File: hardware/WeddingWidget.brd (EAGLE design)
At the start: 25.1 x 50.8 mm, 7 parts, among them J1 AVR_SPI_PRG_6NS, SW1 EVQQ2, SW2 EVQQ2

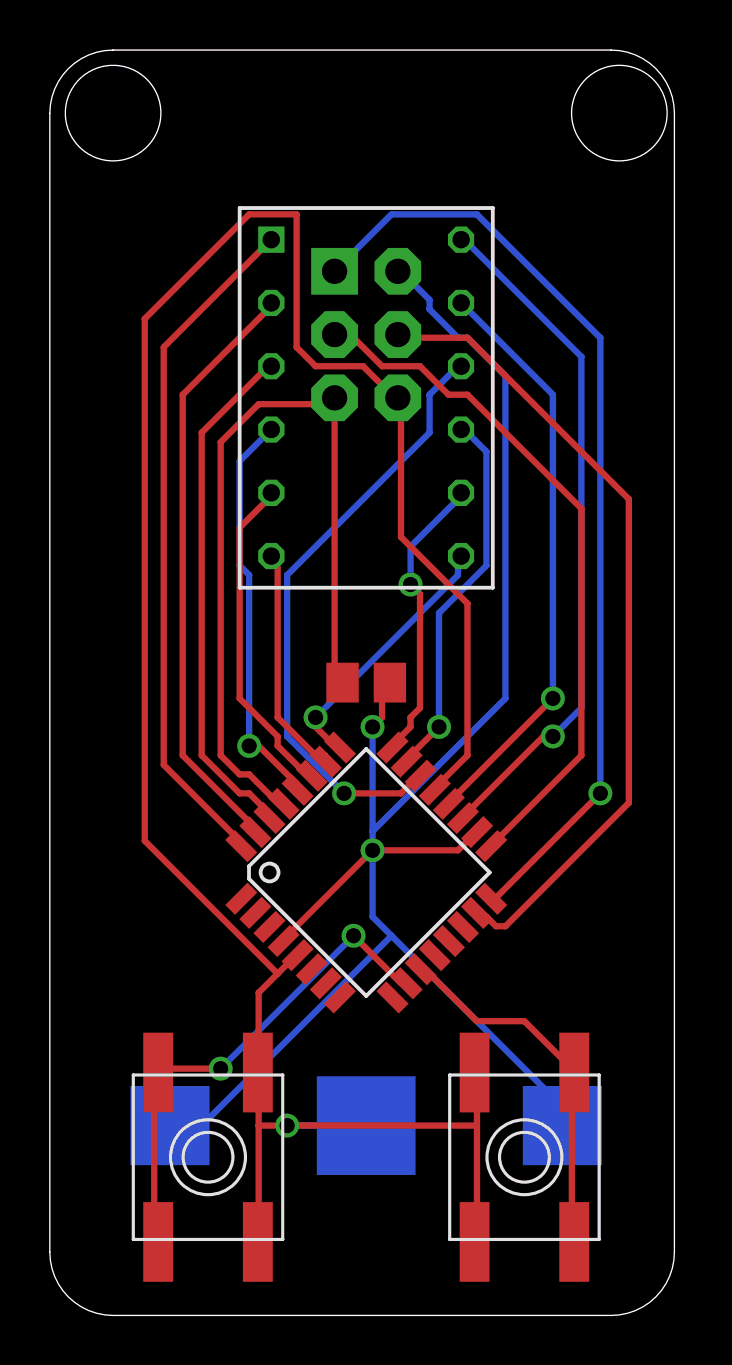
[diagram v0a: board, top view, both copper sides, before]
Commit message: added battery holder and bottom ground plane
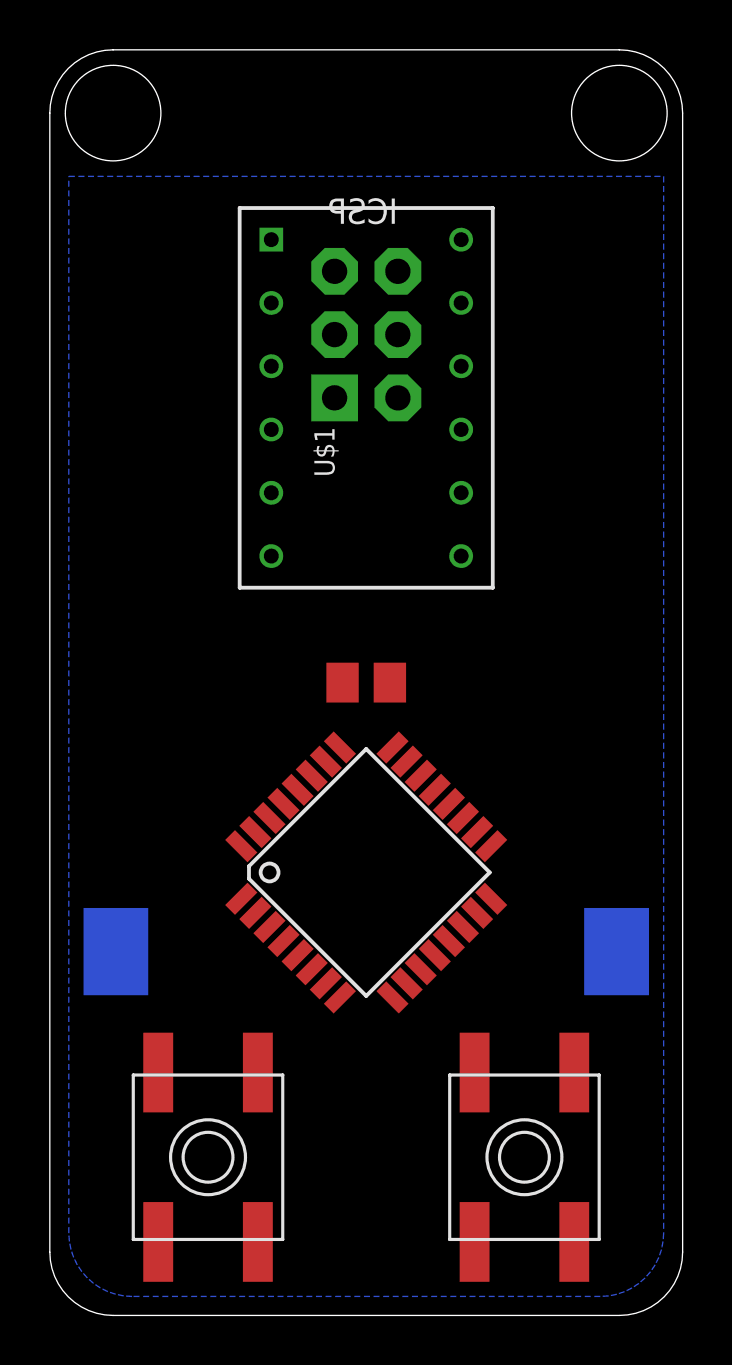
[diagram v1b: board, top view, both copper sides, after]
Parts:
- BAT1: device SparkFun:BATTCON_12MM -> rxtx-labs:BATTCON_12MM
- moved BAT1 6.99 mm to (12.7, 14.6), turned to 0 degrees
- flipped J1 to the bottom, turned to 90 degrees
- turned SW1 to 270 degrees
- turned SW2 to 90 degrees
- renumbered LED1 to U$1
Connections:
- net VCC: now also BAT1.V+; no longer BAT1.PWR@1, BAT1.PWR@2
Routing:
- net GND: track 95.0 -> 0.00 mm, vias 1 -> 0
- net VCC: track 69.7 -> 0.00 mm, vias 2 -> 0
- net MISO: track 38.1 -> 0.00 mm, vias 1 -> 0
- net RST: track 32.7 -> 0.00 mm
- net MOSI: track 32.5 -> 0.00 mm
- net SCK: track 27.9 -> 0.00 mm
- net ROW1: track 27.4 -> 0.00 mm, vias 1 -> 0
- net COL1: track 27.4 -> 0.00 mm
- net COL3: track 24.5 -> 0.00 mm, vias 1 -> 0
- net ROW3: track 24.0 -> 0.00 mm
- net ROW2: track 23.4 -> 0.00 mm, vias 1 -> 0
- net COL2: track 20.7 -> 0.00 mm
- net PCINT22: track 20.0 -> 0.00 mm, vias 2 -> 0
- net ROW5: track 16.2 -> 0.00 mm, vias 1 -> 0
- net ROW4: track 15.1 -> 0.00 mm, vias 1 -> 0
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- added copper zone on layer 16, net GND
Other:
- board size 25.1 x 50.8 mm -> 25.4 x 50.8 mm
- board text added: "ICSP"

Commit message: Hand routed all traces. Ready for prototype boards to be produced.
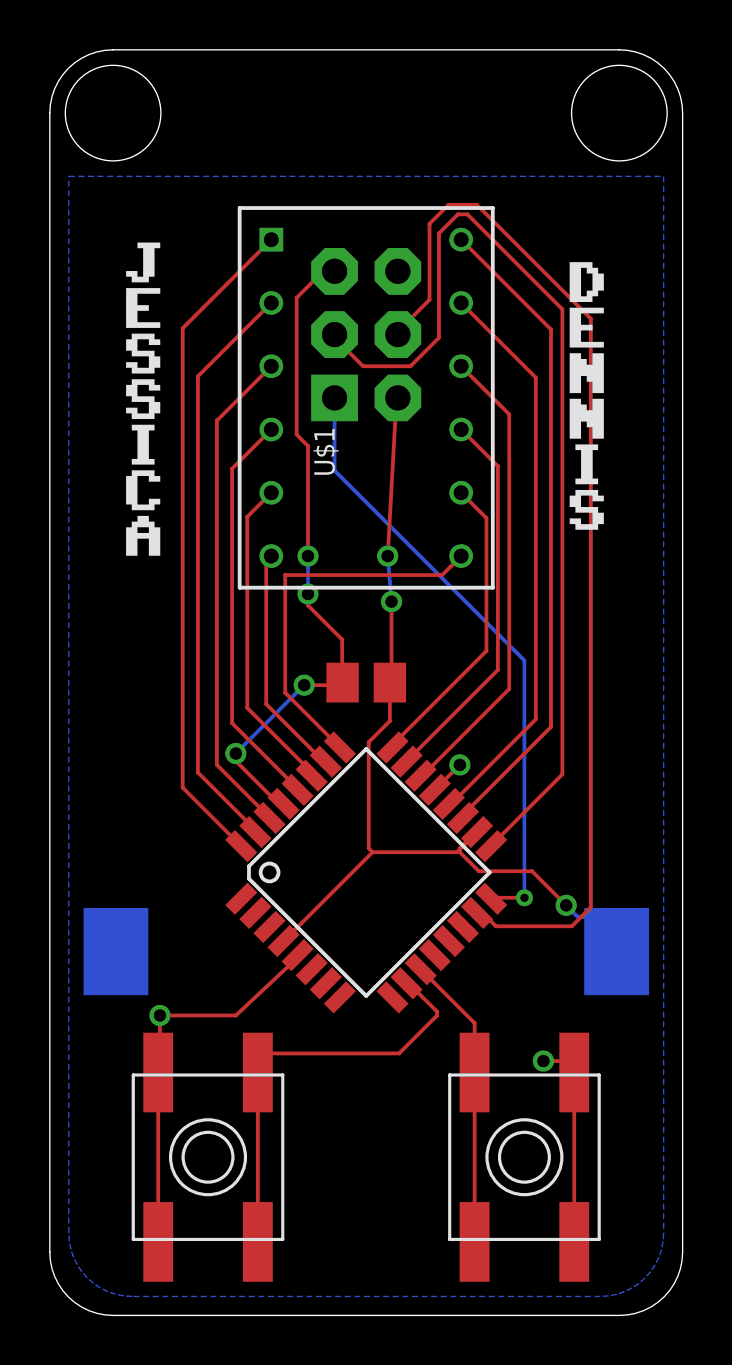
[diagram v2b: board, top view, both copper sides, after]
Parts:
- added U$2: DENNIS, rxtx-labs:DENNIS
- added U$3: JESSICA, rxtx-labs:JESSICA
- added U$4: 23FEB2013, rxtx-labs:23FEB2013
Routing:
- net MOSI: track 0.00 -> 42.3 mm
- net SCK: track 0.00 -> 39.0 mm
- net VCC: track 0.00 -> 38.1 mm, vias 0 -> 3
- net RST: track 0.00 -> 27.1 mm, vias 0 -> 4
- net COL1: track 0.00 -> 26.8 mm
- net ROW1: track 0.00 -> 26.2 mm
- net GND: track 0.00 -> 25.6 mm, vias 0 -> 3
- net MISO: track 0.00 -> 24.6 mm, vias 0 -> 1
- net ROW3: track 0.00 -> 23.4 mm
- net ROW2: track 0.00 -> 22.8 mm
- net COL2: track 0.00 -> 19.9 mm
- net COL3: track 0.00 -> 18.7 mm
- net PCINT22: track 0.00 -> 17.1 mm
- net ROW5: track 0.00 -> 16.2 mm
- net ROW4: track 0.00 -> 15.5 mm
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
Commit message: Dropped bitmapped text for prototype run.
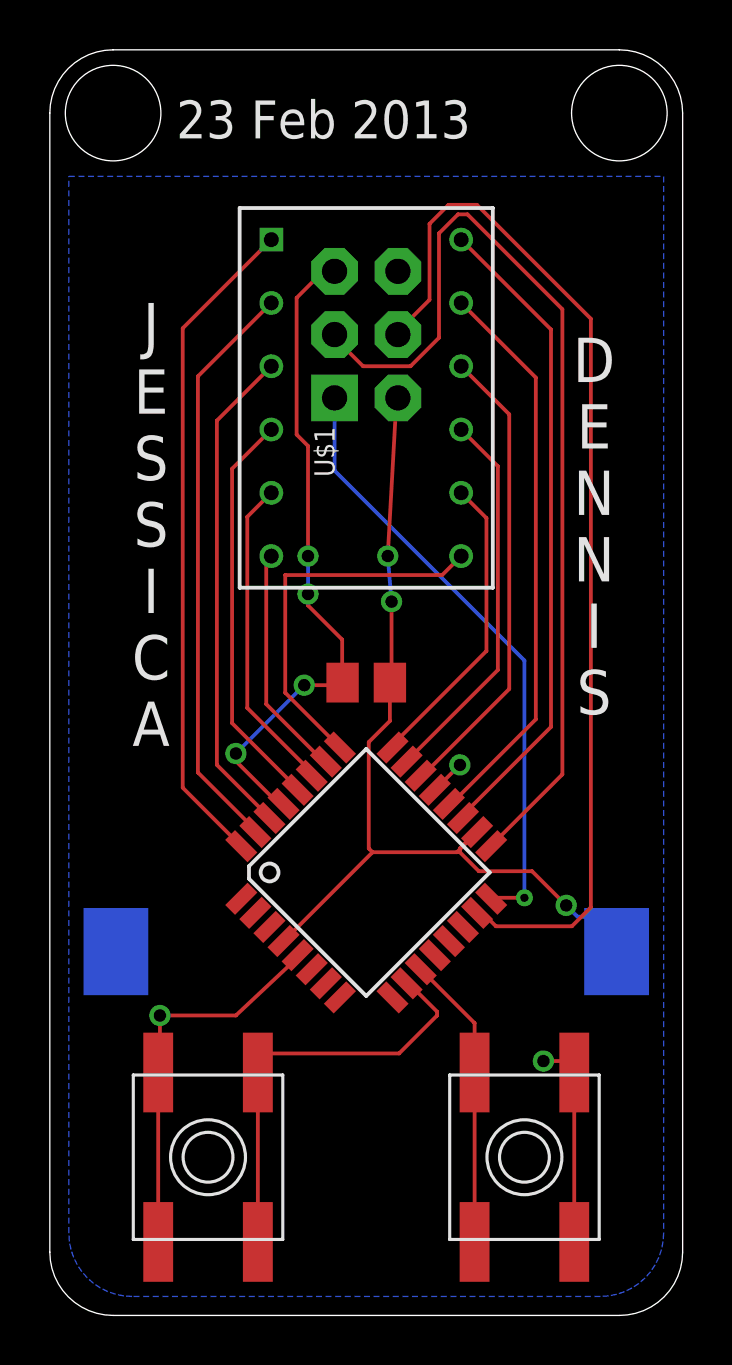
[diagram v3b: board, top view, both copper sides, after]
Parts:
- removed U$2: DENNIS, rxtx-labs:DENNIS
- removed U$3: JESSICA, rxtx-labs:JESSICA
- removed U$4: 23FEB2013, rxtx-labs:23FEB2013
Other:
- board text added: "23 Feb 2013"
- board text added: "D E N N I S"
- board text added: "J E S S I C A"
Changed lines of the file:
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@@
 <layer number="42" name="bRestrict" color="1" fill="10" visible="no" active="yes"/>
 <layer number="43" name="vRestrict" color="2" fill="10" visible="no" active="yes"/>
-<layer number="44" name="Drills" color="7" fill="1" visible="no" active="yes"/>
+<layer number="44" name="Drills" color="7" fill="1" visible="yes" active="yes"/>
 <layer number="45" name="Holes" color="7" fill="1" visible="yes" active="yes"/>
 <layer number="46" name="Milling" color="3" fill="1" visible="no" active="yes"/>
@@
 <hole x="22.86" y="48.26" drill="3.8354"/>
 <text x="13.97" y="43.815" size="1.016" layer="22" rot="MR0">ICSP</text>
+<text x="4.064" y="22.86" size="1.778" layer="21" font="fixed" align="bottom-center">J
+E
+S
+S
+I
+C
+A</text>
+<text x="21.844" y="24.13" size="1.778" layer="21" font="fixed" align="bottom-center">D
+E
+N
+N
+I
+S</text>
+<text x="5.08" y="47.244" size="1.524" layer="21">23 Feb 2013</text>
 </plain>
 <attributes>
@@
 <element name="BAT1" library="rxtx-labs" package="BATTCON_12MM" value="" x="12.7" y="14.605" rot="MR0"/>
 <element name="U$1" library="LiteOn-LED-Matrix" package="LTP-747" value="LTP-747PTH" x="12.7" y="36.83"/>
-<element name="U$2" library="rxtx-labs" package="DENNIS" value="DENNIS" x="20.828" y="31.496"/>
-<element name="U$3" library="rxtx-labs" package="JESSICA" value="JESSICA" x="3.048" y="30.48"/>
-<element name="U$4" library="rxtx-labs" package="23FEB2013" value="23FEB2013" x="22.606" y="3.048" rot="MR0"/>
 </elements>
 <signals>
@@
 </board>
 </drawing>
+<compatibility>
+<note version="6.3" minversion="6.2.2" severity="warning">
+Since Version 6.2.2 text objects can contain more than one line,
+which will not be processed correctly with this version.
+</note>
+</compatibility>
 </eagle>

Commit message: added bitmap text to board
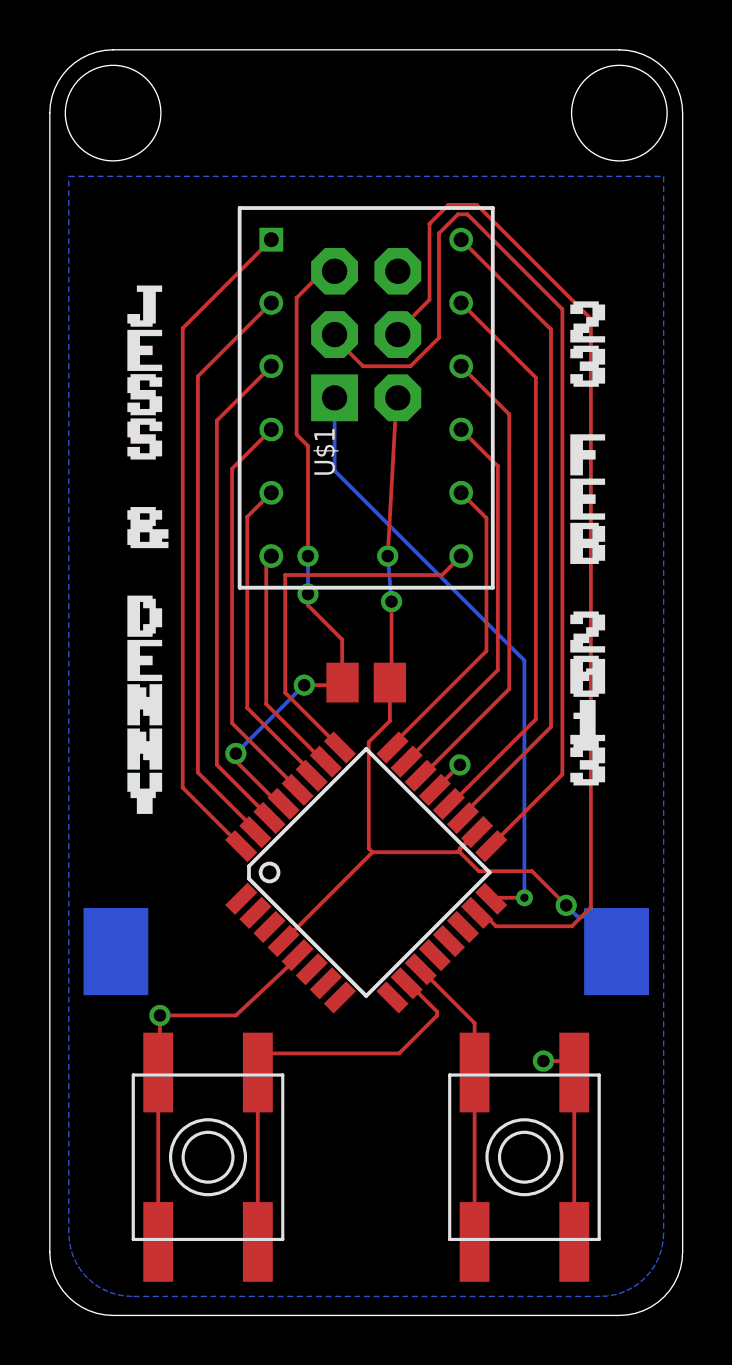
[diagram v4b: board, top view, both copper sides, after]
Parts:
- added U$2: JESS-N-DENNY, rxtx-labs:JESS-N-DENNY
- added U$3: 23FEB2013, rxtx-labs:23FEB2013
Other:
- board text removed: "23 Feb 2013"
- board text removed: "D E N N I S"
- board text removed: "J E S S I C A"
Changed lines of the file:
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@@
 <setting verticaltext="up"/>
 </settings>
-<grid distance="0.1" unitdist="inch" unit="inch" style="dots" multiple="1" display="yes" altdistance="0.01" altunitdist="inch" altunit="inch"/>
+<grid distance="0.1" unitdist="inch" unit="inch" style="dots" multiple="1" display="yes" altdistance="0.05" altunitdist="inch" altunit="inch"/>
 <layers>
 <layer number="1" name="Top" color="4" fill="1" visible="yes" active="yes"/>
@@
 <hole x="22.86" y="48.26" drill="3.8354"/>
 <text x="13.97" y="43.815" size="1.016" layer="22" rot="MR0">ICSP</text>
-<text x="4.064" y="22.86" size="1.778" layer="21" font="fixed" align="bottom-center">J
-E
-S
-S
-I
-C
-A</text>
-<text x="21.844" y="24.13" size="1.778" layer="21" font="fixed" align="bottom-center">D
-E
-N
-N
-I
-S</text>
-<text x="5.08" y="47.244" size="1.524" layer="21">23 Feb 2013</text>
 </plain>
 <attributes>
@@
 <element name="BAT1" library="rxtx-labs" package="BATTCON_12MM" value="" x="12.7" y="14.605" rot="MR0"/>
 <element name="U$1" library="LiteOn-LED-Matrix" package="LTP-747" value="LTP-747PTH" x="12.7" y="36.83"/>
+<element name="U$2" library="rxtx-labs" package="JESS-N-DENNY" value="JESS-N-DENNY" x="3.81" y="20.32"/>
+<element name="U$3" library="rxtx-labs" package="23FEB2013" value="23FEB2013" x="21.59" y="21.59"/>
 </elements>
 <signals>
@@
 </board>
 </drawing>
-<compatibility>
-<note version="6.3" minversion="6.2.2" severity="warning">
-Since Version 6.2.2 text objects can contain more than one line,
-which will not be processed correctly with this version.
-</note>
-</compatibility>
 </eagle>

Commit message: Final design. Sent for manufacturing.
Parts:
- added U$4: HEART, rxtx-labs:HEART
- added U$5: TETRISH, rxtx-labs:TETRISH
- added U$6: TRIFORCE, rxtx-labs:TRIFORCE
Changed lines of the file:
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@@
 <setting verticaltext="up"/>
 </settings>
-<grid distance="0.1" unitdist="inch" unit="inch" style="dots" multiple="1" display="yes" altdistance="0.05" altunitdist="inch" altunit="inch"/>
+<grid distance="0.01" unitdist="inch" unit="inch" style="dots" multiple="1" display="yes" altdistance="0.05" altunitdist="inch" altunit="inch"/>
 <layers>
 <layer number="1" name="Top" color="4" fill="1" visible="yes" active="yes"/>
@@
 <wire x1="25.4" y1="2.54" x2="25.4" y2="48.26" width="0" layer="20"/>
 <wire x1="25.4" y1="48.26" x2="22.86" y2="50.8" width="0" layer="20" curve="90"/>
-<hole x="2.54" y="48.26" drill="3.8354"/>
-<hole x="22.86" y="48.26" drill="3.8354"/>
 <text x="13.97" y="43.815" size="1.016" layer="22" rot="MR0">ICSP</text>
 </plain>
@@
 <element name="U$2" library="rxtx-labs" package="JESS-N-DENNY" value="JESS-N-DENNY" x="3.81" y="20.32"/>
 <element name="U$3" library="rxtx-labs" package="23FEB2013" value="23FEB2013" x="21.59" y="21.59"/>
+<element name="U$4" library="rxtx-labs" package="HEART" value="HEART" x="12.446" y="3.556"/>
+<element name="U$5" library="rxtx-labs" package="TETRISH" value="TETRISH" x="21.844" y="1.27" rot="MR0"/>
+<element name="U$6" library="rxtx-labs" package="TRIFORCE" value="TRIFORCE" x="12.446" y="47.244"/>
 </elements>
 <signals>
